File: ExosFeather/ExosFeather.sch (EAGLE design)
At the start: 21 parts, among them J1 JST_PH_2_PTH, J2 TC_2050_IDC_TOP, J6 CONN_2X1_JST_PA, U1 TVS_USB_TPD4S012, U2 STM32L052KX, U3 TI_CHGR_BQ21040

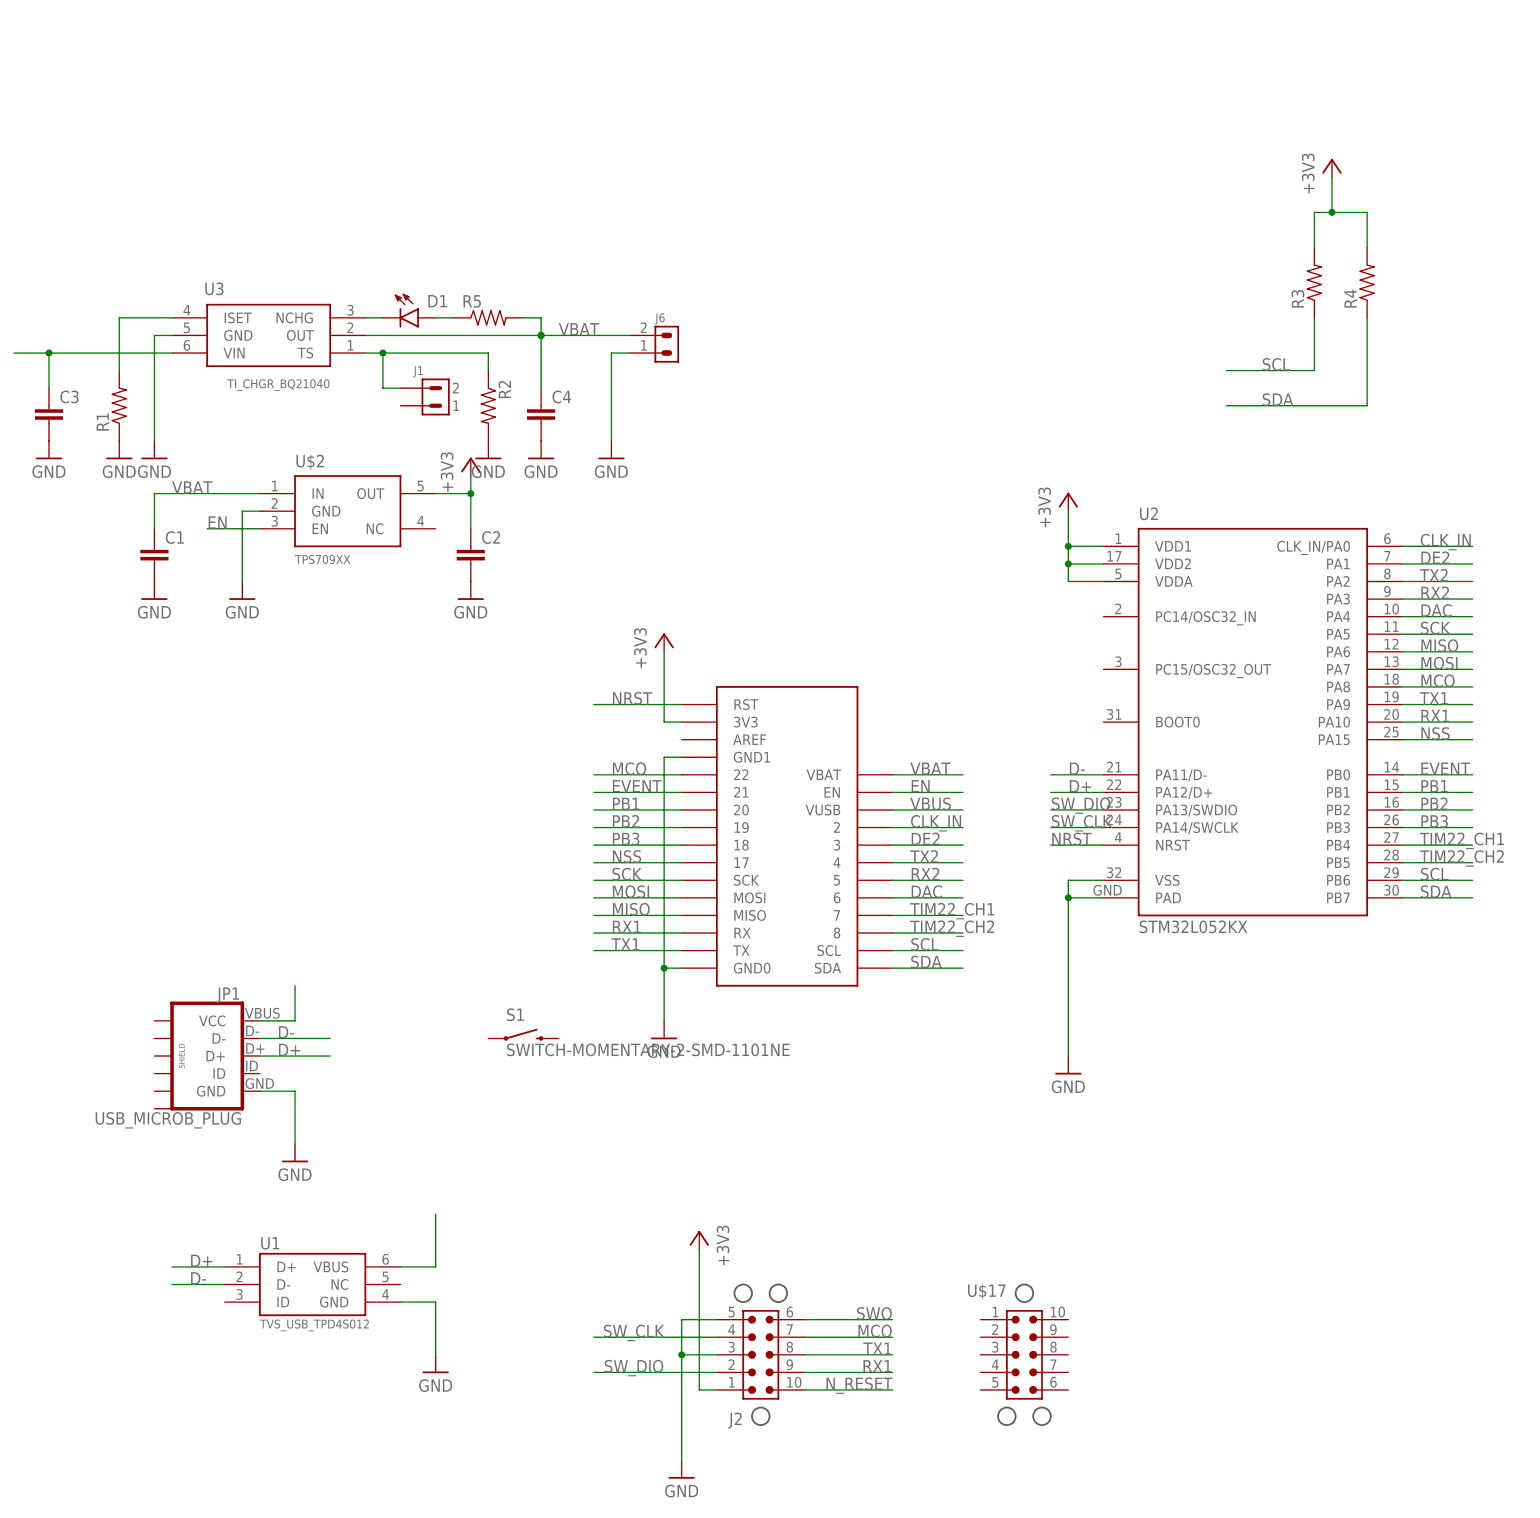
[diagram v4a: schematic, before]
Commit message: updating exosFeather
need to:
1. add jumpers for enable pin & USB power routing
2. pin names
3. decide on PB1 & 2 &3
4. route enable pin
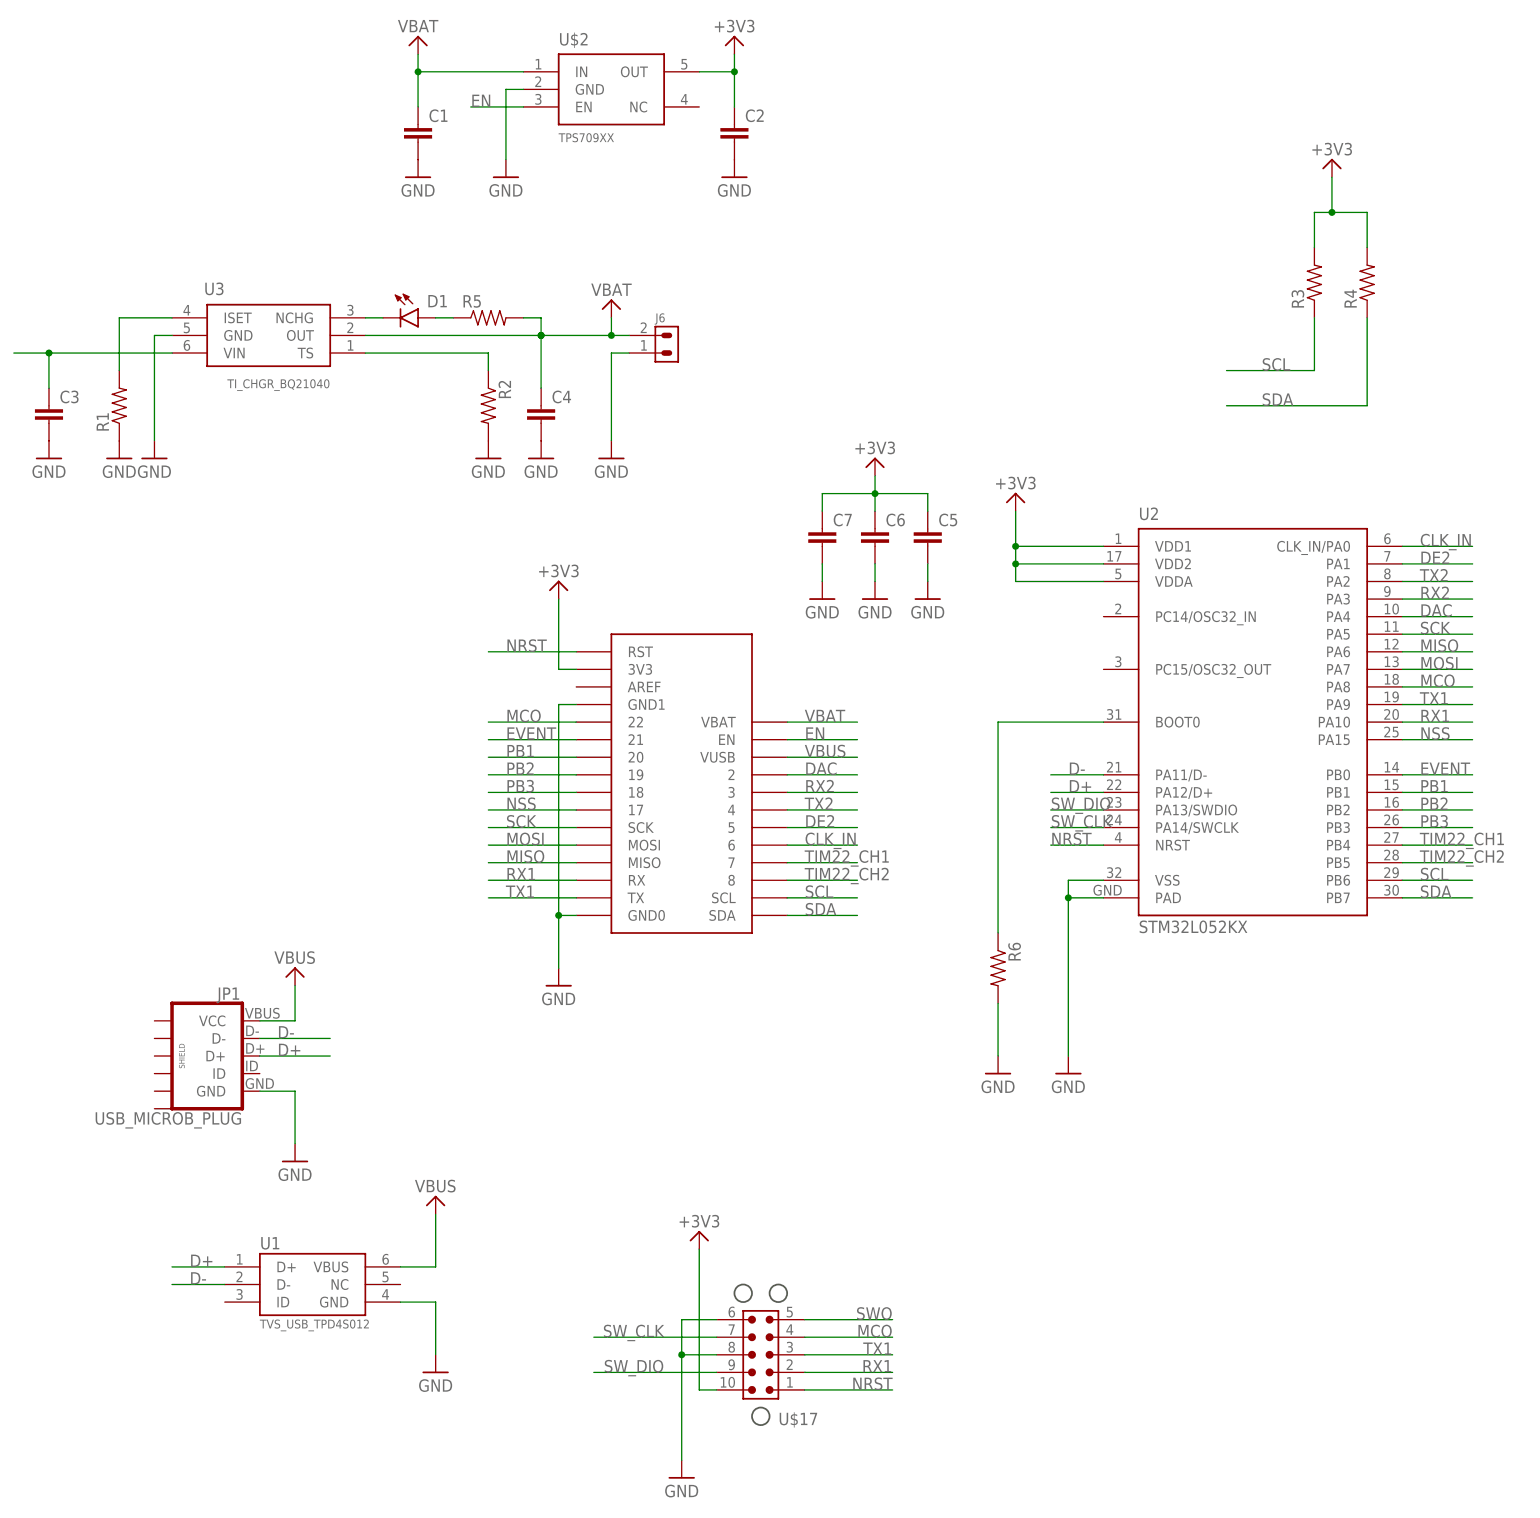
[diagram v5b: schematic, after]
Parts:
- removed J1: JST_PH_2_PTH, stepOSP:JST_PH_2_PTH
- removed J2: TC_2050_IDC_TOP, leaf:TC_2050_IDC_TOP
- removed S1: SWITCH-MOMENTARY-2-SMD-1101NE, SparkFun-Electromechanical:SWITCH-MOMENTARY-2-SMD-1101NE
- added C5, C6, C7: (no value), stepOSP:0603_CAP
- added R6: (no value), stepOSP:0603_RES
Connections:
- removed net N_RESET: J2.10
- new net N$1: R6.1, U2.BOOT0
- net +3V3: now also C5.1, C6.1, C7.1, U$17.10; no longer J2.1
- net CLK_IN: now also U$1.6; no longer U$1.2
- net DAC: now also U$1.2; no longer U$1.6
- net DE2: now also U$1.5; no longer U$1.3
- net GND: now also C5.2, C6.2, C7.2, R6.2, U$17.6, U$17.8; no longer J2.3, J2.5
- net MCO: now also U$17.4; no longer J2.7
- net N$3: no longer J1.2
- net NRST: now also U$17.1
- net RX1: now also U$17.2; no longer J2.9
- net RX2: now also U$1.3; no longer U$1.5
- net SWO: now also U$17.5; no longer J2.6
- net SW_CLK: now also U$17.7; no longer J2.4
- net SW_DIO: now also U$17.9; no longer J2.2
- net TX1: now also U$17.3; no longer J2.8
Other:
- moved on the sheet: C1, C2, U$17, U$2
